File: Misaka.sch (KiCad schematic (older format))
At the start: 7 parts, among them J1 Battery, SW1 SW_DIP_x03, U2 ATmega2560-16AU, Y1 CSTLS16M0X51-B0

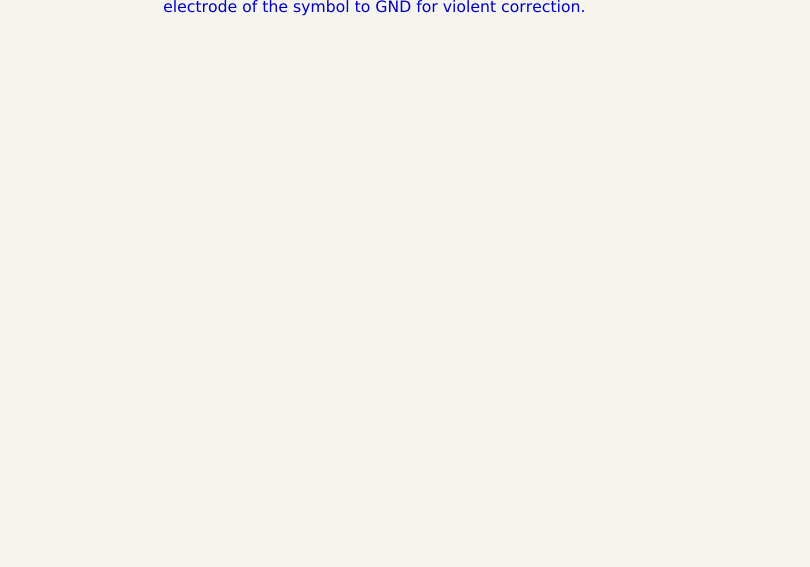
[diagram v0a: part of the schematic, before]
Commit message: Test Pin
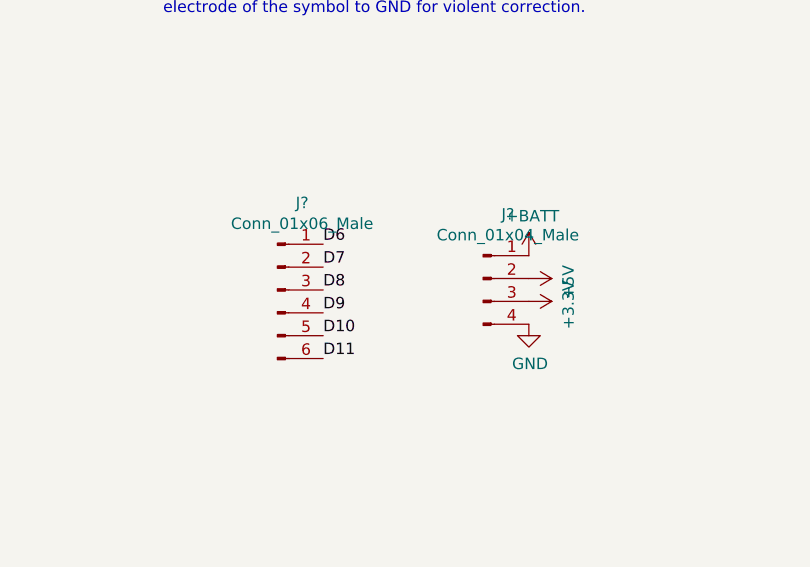
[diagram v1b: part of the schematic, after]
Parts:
- added J?: Conn_01x06_Male, symbol Connector:Conn_01x06_Male
- added J?: Conn_01x04_Male, symbol Connector:Conn_01x04_Male
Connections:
- net +3V3: now also J?.3 (Pin_3)
- net +5V: now also J?.2 (Pin_2)
- net +BATT: now also J?.1 (Pin_1)
- net D10: now also J?.5 (Pin_5)
- net D11: now also J?.6 (Pin_6)
- net D6: now also J?.1 (Pin_1)
- net D7: now also J?.2 (Pin_2)
- net D8: now also J?.3 (Pin_3)
- net D9: now also J?.4 (Pin_4)
- net GND: now also J?.4 (Pin_4)
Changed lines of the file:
@@
 Wire Wire Line
 	1300 2650 1400 2650
+$Comp
+L Connector:Conn_01x06_Male J?
+U 1 1 5E92E8D4
+P 1700 4600
+F 0 "J?" H 1808 4981 50  0000 C CNN
+F 1 "Conn_01x06_Male" H 1808 4890 50  0000 C CNN
+F 2 "" H 1700 4600 50  0001 C CNN
+F 3 "~" H 1700 4600 50  0001 C CNN
+	1    1700 4600
+	1    0    0    -1
+$EndComp
+Text Label 1900 4400 0    50   ~ 0
+D6
+Text Label 1900 4500 0    50   ~ 0
+D7
+Text Label 1900 4600 0    50   ~ 0
+D8
+Text Label 1900 4700 0    50   ~ 0
+D9
+Text Label 1900 4800 0    50   ~ 0
+D10
+Text Label 1900 4900 0    50   ~ 0
+D11
+$Comp
+L Connector:Conn_01x04_Male J?
+U 1 1 5E935723
+P 2600 4550
+F 0 "J?" H 2708 4831 50  0000 C CNN
+F 1 "Conn_01x04_Male" H 2708 4740 50  0000 C CNN
+F 2 "" H 2600 4550 50  0001 C CNN
+F 3 "~" H 2600 4550 50  0001 C CNN
+	1    2600 4550
+	1    0    0    -1
+$EndComp
+$Comp
+L power:+5V #PWR?
+U 1 1 5E93710C
+P 2800 4550
+F 0 "#PWR?" H 2800 4400 50  0001 C CNN
+F 1 "+5V" H 2815 4723 50  0000 C CNN
+F 2 "" H 2800 4550 50  0001 C CNN
+F 3 "" H 2800 4550 50  0001 C CNN
+	1    2800 4550
+	0    1    1    0
+$EndComp
+$Comp
+L power:GND #PWR?
+U 1 1 5E9388D9
+P 2800 4750
+F 0 "#PWR?" H 2800 4500 50  0001 C CNN
+F 1 "GND" H 2805 4577 50  0000 C CNN
+F 2 "" H 2800 4750 50  0001 C CNN
+F 3 "" H 2800 4750 50  0001 C CNN
+	1    2800 4750
+	1    0    0    -1
+$EndComp
+$Comp
+L power:+3.3V #PWR?
+U 1 1 5E9395EB
+P 2800 4650
+F 0 "#PWR?" H 2800 4500 50  0001 C CNN
+F 1 "+3.3V" H 2815 4823 50  0000 C CNN
+F 2 "" H 2800 4650 50  0001 C CNN
+F 3 "" H 2800 4650 50  0001 C CNN
+	1    2800 4650
+	0    1    1    0
+$EndComp
+$Comp
+L power:+BATT #PWR?
+U 1 1 5E93C551
+P 2800 4450
+F 0 "#PWR?" H 2800 4300 50  0001 C CNN
+F 1 "+BATT" H 2815 4623 50  0000 C CNN
+F 2 "" H 2800 4450 50  0001 C CNN
+F 3 "" H 2800 4450 50  0001 C CNN
+	1    2800 4450
+	1    0    0    -1
+$EndComp
 $EndSCHEMATC

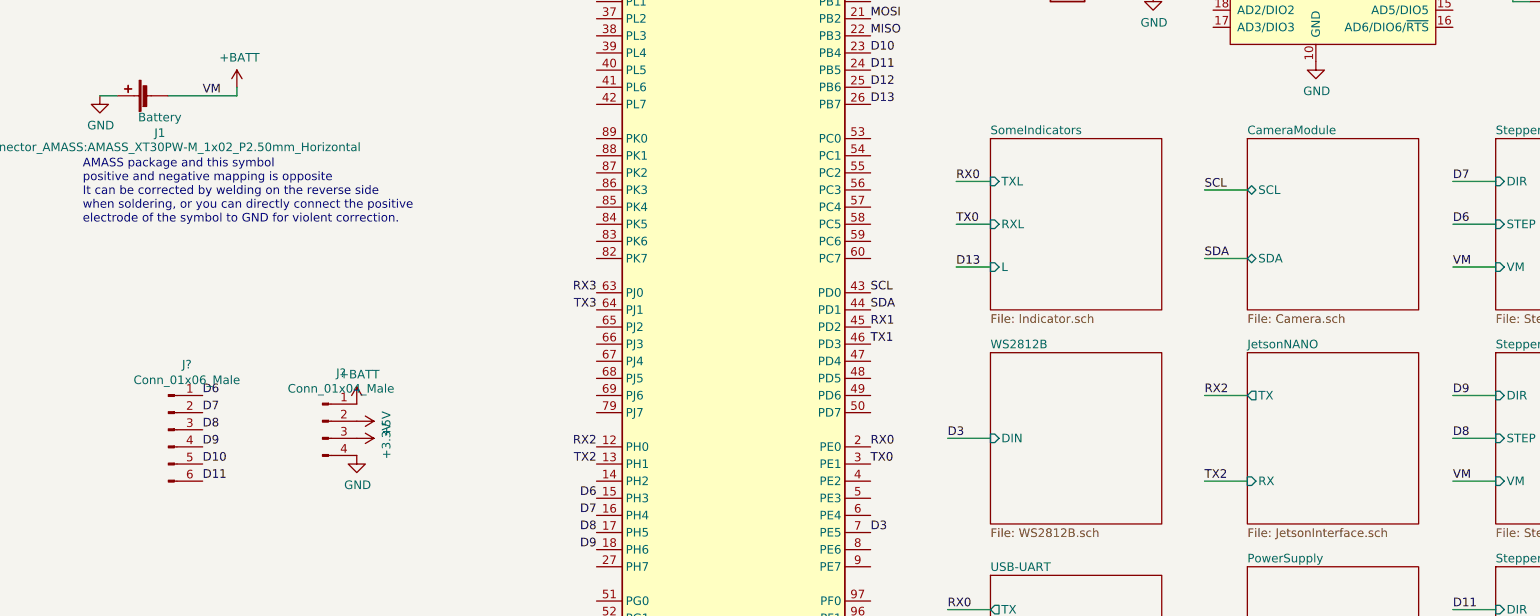
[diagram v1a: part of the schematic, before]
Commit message: DEL Camera
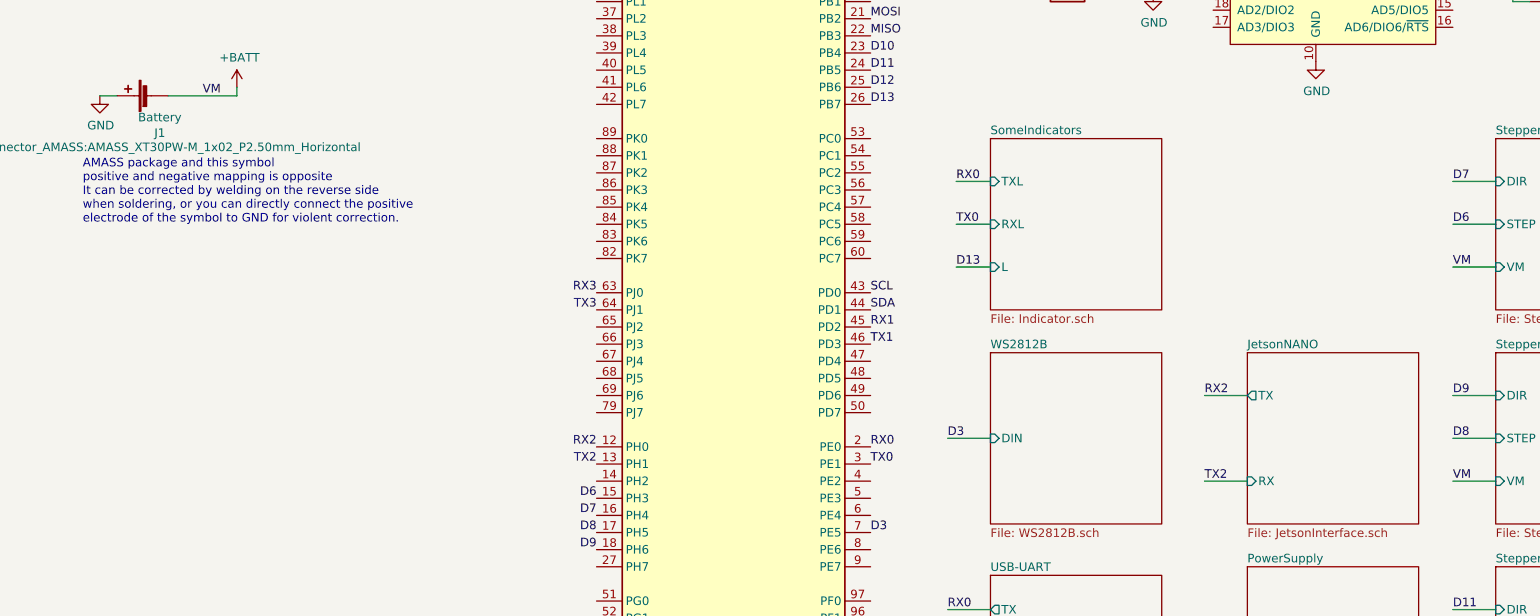
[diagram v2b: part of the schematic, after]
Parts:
- removed J?: Conn_01x06_Male, symbol Connector:Conn_01x06_Male
- removed J?: Conn_01x04_Male, symbol Connector:Conn_01x04_Male
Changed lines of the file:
@@
 $Descr A4 11693 8268
 encoding utf-8
-Sheet 1 10
+Sheet 1 9
 Title ""
 Date ""
@@
 Wire Wire Line
 	7200 2050 7450 2050
-$Sheet
-S 8000 2900 1000 1000
-U 5E68B603
-F0 "CameraModule" 50
-F1 "Camera.sch" 50
-F2 "SCL" B L 8000 3200 50
-F3 "SDA" B L 8000 3600 50
-$EndSheet
 Text Label 5800 3800 0    50   ~ 0
 SCL
 Text Label 5800 3900 0    50   ~ 0
-SDA
-Wire Wire Line
-	8000 3200 7750 3200
-Wire Wire Line
-	8000 3600 7750 3600
-Text Label 7750 3200 0    50   ~ 0
-SCL
-Text Label 7750 3600 0    50   ~ 0
 SDA
 $Sheet
@@
 Wire Wire Line
 	1300 2650 1400 2650
-$Comp
-L Connector:Conn_01x06_Male J?
-U 1 1 5E92E8D4
-P 1700 4600
-F 0 "J?" H 1808 4981 50  0000 C CNN
-F 1 "Conn_01x06_Male" H 1808 4890 50  0000 C CNN
-F 2 "" H 1700 4600 50  0001 C CNN
-F 3 "~" H 1700 4600 50  0001 C CNN
-	1    1700 4600
-	1    0    0    -1
-$EndComp
-Text Label 1900 4400 0    50   ~ 0
-D6
-Text Label 1900 4500 0    50   ~ 0
-D7
-Text Label 1900 4600 0    50   ~ 0
-D8
-Text Label 1900 4700 0    50   ~ 0
-D9
-Text Label 1900 4800 0    50   ~ 0
-D10
-Text Label 1900 4900 0    50   ~ 0
-D11
-$Comp
-L Connector:Conn_01x04_Male J?
-U 1 1 5E935723
-P 2600 4550
-F 0 "J?" H 2708 4831 50  0000 C CNN
-F 1 "Conn_01x04_Male" H 2708 4740 50  0000 C CNN
-F 2 "" H 2600 4550 50  0001 C CNN
-F 3 "~" H 2600 4550 50  0001 C CNN
-	1    2600 4550
-	1    0    0    -1
-$EndComp
-$Comp
-L power:+5V #PWR?
-U 1 1 5E93710C
-P 2800 4550
-F 0 "#PWR?" H 2800 4400 50  0001 C CNN
-F 1 "+5V" H 2815 4723 50  0000 C CNN
-F 2 "" H 2800 4550 50  0001 C CNN
-F 3 "" H 2800 4550 50  0001 C CNN
-	1    2800 4550
-	0    1    1    0
-$EndComp
-$Comp
-L power:GND #PWR?
-U 1 1 5E9388D9
-P 2800 4750
-F 0 "#PWR?" H 2800 4500 50  0001 C CNN
-F 1 "GND" H 2805 4577 50  0000 C CNN
-F 2 "" H 2800 4750 50  0001 C CNN
-F 3 "" H 2800 4750 50  0001 C CNN
-	1    2800 4750
-	1    0    0    -1
-$EndComp
-$Comp
-L power:+3.3V #PWR?
-U 1 1 5E9395EB
-P 2800 4650
-F 0 "#PWR?" H 2800 4500 50  0001 C CNN
-F 1 "+3.3V" H 2815 4823 50  0000 C CNN
-F 2 "" H 2800 4650 50  0001 C CNN
-F 3 "" H 2800 4650 50  0001 C CNN
-	1    2800 4650
-	0    1    1    0
-$EndComp
-$Comp
-L power:+BATT #PWR?
-U 1 1 5E93C551
-P 2800 4450
-F 0 "#PWR?" H 2800 4300 50  0001 C CNN
-F 1 "+BATT" H 2815 4623 50  0000 C CNN
-F 2 "" H 2800 4450 50  0001 C CNN
-F 3 "" H 2800 4450 50  0001 C CNN
-	1    2800 4450
-	1    0    0    -1
-$EndComp
 $EndSCHEMATC

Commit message: DEL LED MS123
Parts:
- removed SW1: SW_DIP_x03, Button_Switch_SMD:SW_DIP_SPSTx03_Slide_6.7x9.18mm_W8.61mm_P2.54mm_LowProfile, symbol Switch:SW_DIP_x03
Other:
- moved on the sheet: J1
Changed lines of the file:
@@
 $Descr A4 11693 8268
 encoding utf-8
-Sheet 1 9
+Sheet 1 8
 Title ""
 Date ""
@@
 MS3
 $Comp
-L Switch:SW_DIP_x03 SW1
-U 1 1 5E63CD4E
-P 9950 2100
-F 0 "SW1" H 9950 2567 50  0000 C CNN
-F 1 "SW_DIP_x03" H 9950 2476 50  0000 C CNN
-F 2 "Button_Switch_SMD:SW_DIP_SPSTx03_Slide_6.7x9.18mm_W8.61mm_P2.54mm_LowProfile" H 9950 2100 50  0001 C CNN
-F 3 "~" H 9950 2100 50  0001 C CNN
-	1    9950 2100
-	1    0    0    -1
-$EndComp
-$Comp
-L power:+5V #PWR0113
-U 1 1 5E63F269
-P 9550 1800
-F 0 "#PWR0113" H 9550 1650 50  0001 C CNN
-F 1 "+5V" H 9565 1973 50  0000 C CNN
-F 2 "" H 9550 1800 50  0001 C CNN
-F 3 "" H 9550 1800 50  0001 C CNN
-	1    9550 1800
-	1    0    0    -1
-$EndComp
-Wire Wire Line
-	9550 1800 9550 1900
-Wire Wire Line
-	9550 1900 9650 1900
-Wire Wire Line
-	9550 1900 9550 2000
-Wire Wire Line
-	9550 2000 9650 2000
-Connection ~ 9550 1900
-Wire Wire Line
-	9550 2000 9550 2100
-Wire Wire Line
-	9550 2100 9650 2100
-Connection ~ 9550 2000
-Wire Wire Line
-	10250 1900 10500 1900
-Wire Wire Line
-	10250 2000 10500 2000
-Wire Wire Line
-	10250 2100 10500 2100
-Text Label 10500 1900 2    50   ~ 0
-MS1
-Text Label 10500 2000 2    50   ~ 0
-MS2
-Text Label 10500 2100 2    50   ~ 0
-MS3
-$Comp
 L power:GND #PWR0127
 U 1 1 5E64EFCB
@@
 Text Label 5800 3900 0    50   ~ 0
 SDA
-$Sheet
-S 6500 4150 1000 1000
-U 5E6D783B
-F0 "WS2812B" 50
-F1 "WS2812B.sch" 50
-F2 "DIN" I L 6500 4650 50
-$EndSheet
 Text Label 5800 5200 0    50   ~ 0
 D3
-Wire Wire Line
-	6500 4650 6250 4650
-Text Label 6250 4650 0    50   ~ 0
-D3
-$Sheet
-S 6500 2900 1000 1000
+$Sheet
+S 6500 4150 1000 1000
 U 5E76060A
 F0 "SomeIndicators" 50
 F1 "Indicator.sch" 50
-F2 "TXL" I L 6500 3150 50
-F3 "RXL" I L 6500 3400 50
-F4 "L" I L 6500 3650 50
-$EndSheet
-Wire Wire Line
-	6500 3150 6300 3150
-Wire Wire Line
-	6500 3400 6300 3400
-Wire Wire Line
-	6500 3650 6300 3650
-Text Label 6300 3400 0    50   ~ 0
+F2 "TXL" I L 6500 4400 50
+F3 "RXL" I L 6500 4650 50
+F4 "L" I L 6500 4900 50
+$EndSheet
+Wire Wire Line
+	6500 4400 6300 4400
+Wire Wire Line
+	6500 4650 6300 4650
+Wire Wire Line
+	6500 4900 6300 4900
+Text Label 6300 4650 0    50   ~ 0
 TX0
-Text Label 6300 3150 0    50   ~ 0
+Text Label 6300 4400 0    50   ~ 0
 RX0
-Text Label 6300 3650 0    50   ~ 0
+Text Label 6300 4900 0    50   ~ 0
 D13
 Text Label 7800 1450 2    50   ~ 0
@@
 $EndSheet
 Wire Wire Line
-	1700 2650 2100 2650
+	7400 3050 7800 3050
 $Comp
 L power:GND #PWR0117
 U 1 1 5E622AF8
-P 1300 2650
-F 0 "#PWR0117" H 1300 2400 50  0001 C CNN
-F 1 "GND" H 1305 2477 50  0000 C CNN
-F 2 "" H 1300 2650 50  0001 C CNN
-F 3 "" H 1300 2650 50  0001 C CNN
-	1    1300 2650
-	1    0    0    -1
-$EndComp
-Text Label 1900 2650 0    50   ~ 0
+P 7000 3050
+F 0 "#PWR0117" H 7000 2800 50  0001 C CNN
+F 1 "GND" H 7005 2877 50  0000 C CNN
+F 2 "" H 7000 3050 50  0001 C CNN
+F 3 "" H 7000 3050 50  0001 C CNN
+	1    7000 3050
+	1    0    0    -1
+$EndComp
+Text Label 7600 3050 0    50   ~ 0
 VM
 Wire Wire Line
-	2100 2650 2100 2600
+	7800 3050 7800 3000
 $Comp
 L power:+BATT #PWR0152
 U 1 1 5E62480E
-P 2100 2600
-F 0 "#PWR0152" H 2100 2450 50  0001 C CNN
-F 1 "+BATT" H 2115 2773 50  0000 C CNN
-F 2 "" H 2100 2600 50  0001 C CNN
-F 3 "" H 2100 2600 50  0001 C CNN
-	1    2100 2600
+P 7800 3000
+F 0 "#PWR0152" H 7800 2850 50  0001 C CNN
+F 1 "+BATT" H 7815 3173 50  0000 C CNN
+F 2 "" H 7800 3000 50  0001 C CNN
+F 3 "" H 7800 3000 50  0001 C CNN
+	1    7800 3000
 	1    0    0    -1
 $EndComp
 Text Label 9200 1450 0    50   ~ 0
 RX1
-Text Notes 1200 3400 0    50   ~ 0
+Text Notes 6900 3800 0    50   ~ 0
 AMASS package and this symbol \npositive and negative mapping is opposite\nIt can be corrected by welding on the reverse side\nwhen soldering, or you can directly connect the positive \nelectrode of the symbol to GND for violent correction.
 $Comp
 L Device:Battery_Cell J1
 U 1 1 5E620D8E
-P 1600 2650
-F 0 "J1" V 1383 2600 50  0000 C CNN
-F 1 "Battery" V 1474 2600 50  0000 C CNN
-F 2 "Connector_AMASS:AMASS_XT30PW-M_1x02_P2.50mm_Horizontal" V 1300 2550 50  0000 C CNN
-F 3 "~" H 1600 2600 50  0001 C CNN
-	1    1600 2650
+P 7300 3050
+F 0 "J1" V 7083 3000 50  0000 C CNN
+F 1 "Battery" V 7174 3000 50  0000 C CNN
+F 2 "Connector_AMASS:AMASS_XT30PW-M_1x02_P2.50mm_Horizontal" V 7000 2950 50  0000 C CNN
+F 3 "~" H 7300 3000 50  0001 C CNN
+	1    7300 3050
 	0    -1   -1   0
 $EndComp
 Wire Wire Line
-	1300 2650 1400 2650
+	7000 3050 7100 3050
 $EndSCHEMATC

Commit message: except GND
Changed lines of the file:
@@
 Text Label 5800 4800 0    50   ~ 0
 TX0
-Wire Wire Line
-	10450 3150 10700 3150
-Wire Wire Line
-	10450 3400 10700 3400
-Wire Wire Line
-	10450 3650 10700 3650
-Wire Wire Line
-	10450 4400 10700 4400
-Wire Wire Line
-	10450 4650 10700 4650
-Wire Wire Line
-	10450 4900 10700 4900
-Wire Wire Line
-	10450 5650 10700 5650
-Wire Wire Line
-	10450 5900 10700 5900
-Wire Wire Line
-	10450 6150 10700 6150
-Text Label 10700 3150 2    50   ~ 0
-MS1
-Text Label 10700 3400 2    50   ~ 0
-MS2
-Text Label 10700 3650 2    50   ~ 0
-MS3
-Text Label 10700 4400 2    50   ~ 0
-MS1
-Text Label 10700 5650 2    50   ~ 0
-MS1
-Text Label 10700 4650 2    50   ~ 0
-MS2
-Text Label 10700 5900 2    50   ~ 0
-MS2
-Text Label 10700 4900 2    50   ~ 0
-MS3
-Text Label 10700 6150 2    50   ~ 0
-MS3
 $Comp
 L power:GND #PWR0127
